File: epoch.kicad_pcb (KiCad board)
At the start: 4 copper layers, 28 x 34 mm, 36 parts, among them J1 USB_OTG, J2 CONN_01X05, P3 CONN_01X10, SW1 SW_Reset, SW2 SW_Up, SW3 SW_Middle, SW4 SW_Down, U1 MIC5219-3.3BM5, U2 ATSAMD21Ennc-AU, U3 DS3231MZ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

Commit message: Final connections
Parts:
- REF** (x4): footprint Connectors:1pin -> Connectors:1pin_nosilk
- SW1: footprint Buttons_Switches_SMD:SW_SPST_SKTDLDE010 -> Buttons_Switches_SMD:SW_SPST_B3U-3000P
- moved C4 38.7 mm to (121.7, 77.2), turned to 180 degrees
- moved R1 34.5 mm to (123.3, 79.2), turned to 180 degrees
- moved SW1 31.6 mm to (128.1, 79.9), turned to 270 degrees
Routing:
- net RESET: track 25.2 -> 44.5 mm, vias 2 -> 4
- net SCL: track 22.5 -> 31.7 mm, vias 2 -> 4
- net (+3.3): track 13.9 -> 21.1 mm, vias 0 -> 2
- net Net-(R1-Pad1): track 0.00 -> 3.95 mm
- net SPI_SI: track 28.7 -> 30.3 mm
- net SPI_CLK: track 21.3 -> 22.7 mm
- net (GND): track 33.6 -> 34.5 mm, vias 14 -> 15

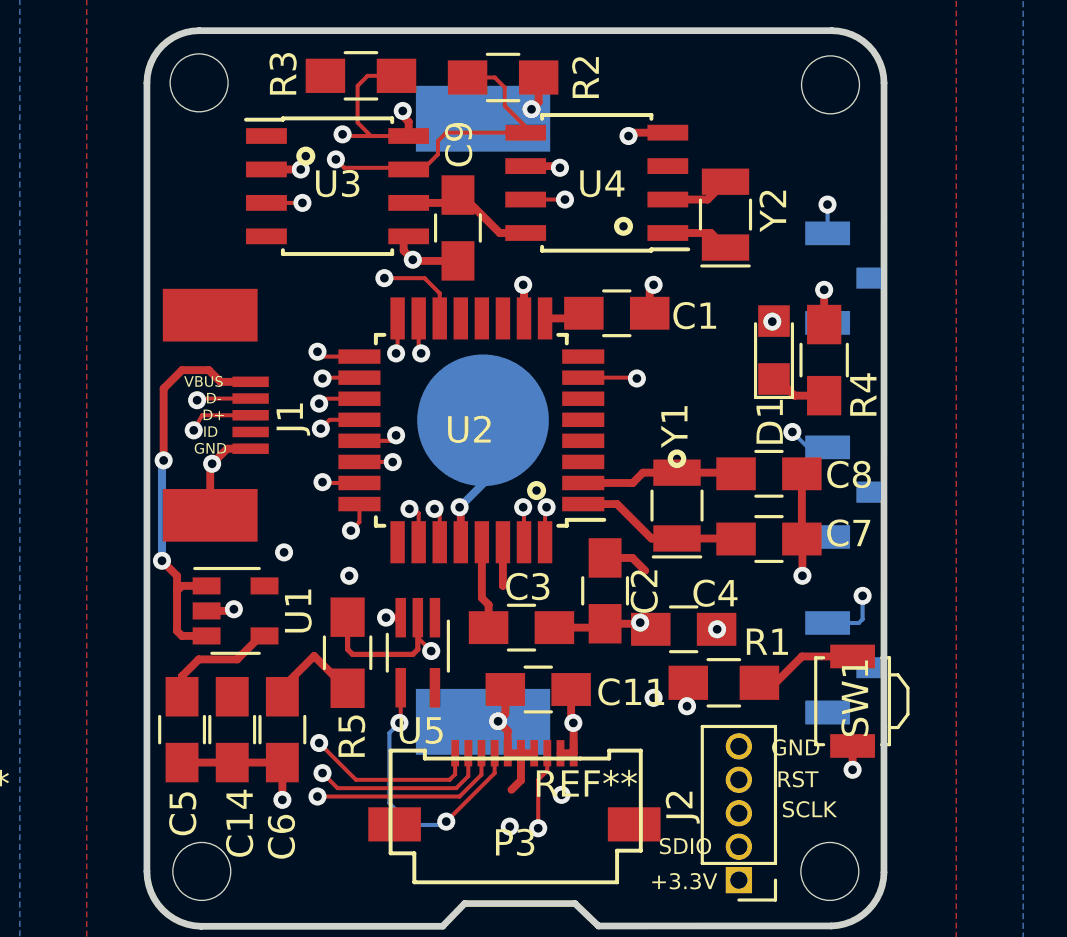
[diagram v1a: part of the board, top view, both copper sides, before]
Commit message: New buttons
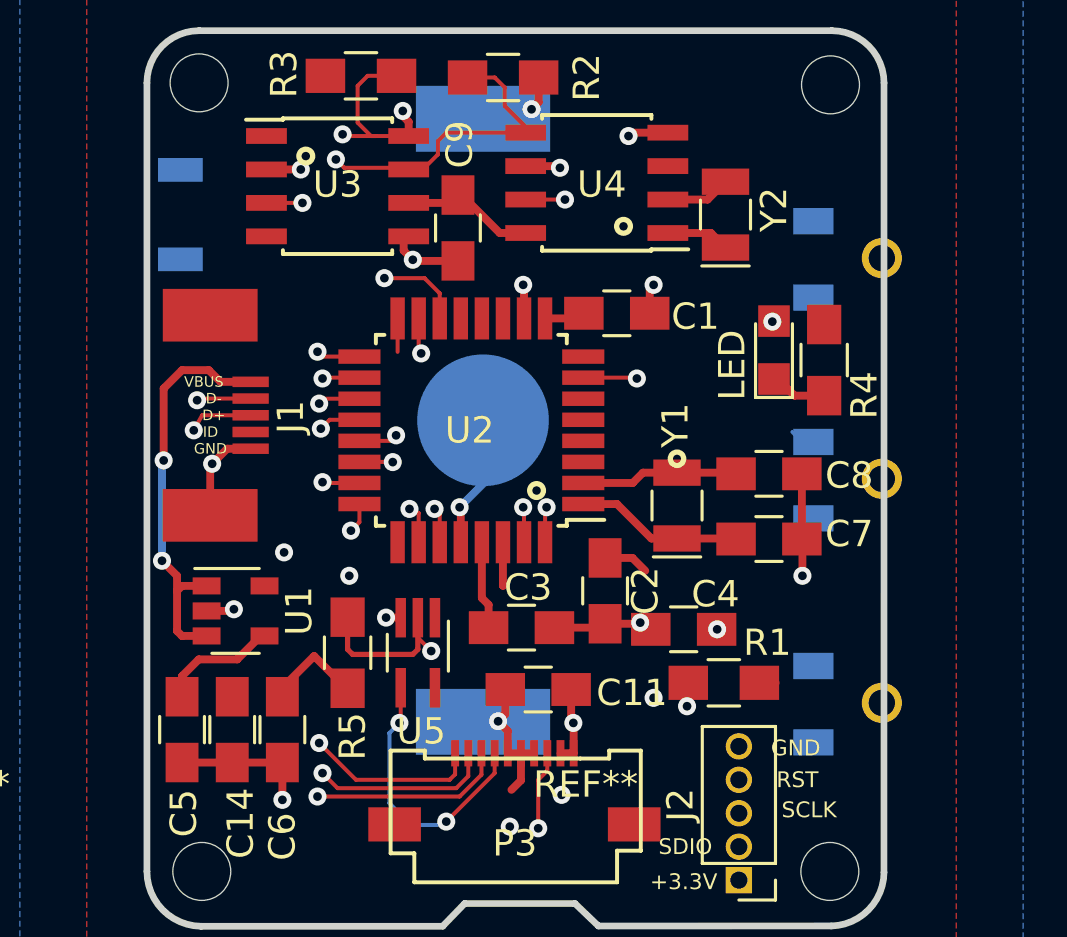
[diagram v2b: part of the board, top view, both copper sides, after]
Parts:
- SW1: moved to B.Cu
- SW2, SW3, SW4: footprint Buttons_Switches_SMD:SW_SPST_B3U-1100P -> Buttons_Switches_SMD:SW_SPDT_EBAY_3PIN_VERT
- moved SW1 31.5 mm to (102.6, 61.5)
- moved SW4 1.54 mm to (127.3, 80.0), turned to 90 degrees
- moved SW2 1.08 mm to (127.3, 63.1), turned to 90 degrees
- moved SW3 0.92 mm to (127.3, 71.5), turned to 90 degrees
- renumbered D1 to LED
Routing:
- net BUT_MID: track 19.5 -> 1.27 mm, vias 2 -> 0
- net (no net): track 0.00 -> 16.1 mm
- net BUT_UP: track 20.2 -> 6.58 mm, vias 2 -> 1
- net BUT_DWN: track 26.7 -> 16.2 mm, vias 2 -> 1
- net Net-(R1-Pad1): track 3.95 -> 0.62 mm
- net (GND): track 34.5 -> 33.9 mm, vias 15 -> 13

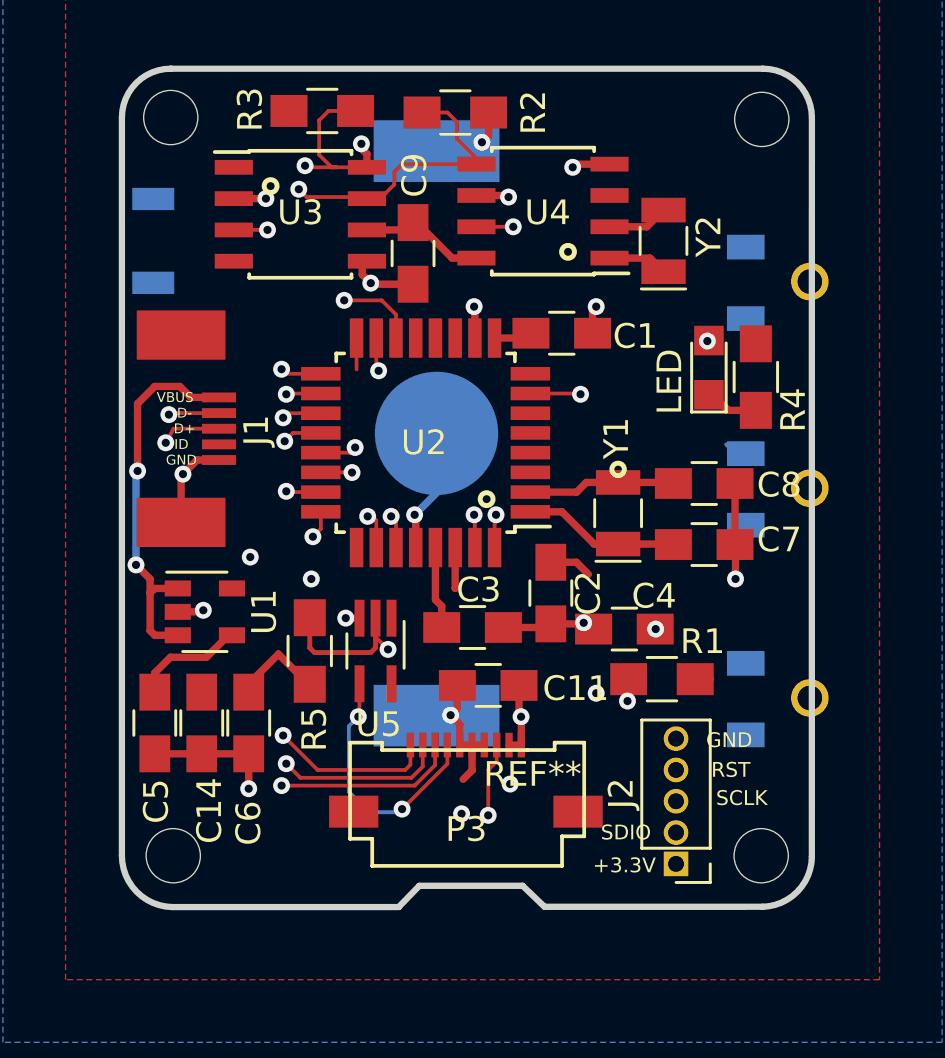
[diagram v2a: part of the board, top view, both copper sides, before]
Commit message: Update all buttons and re-route
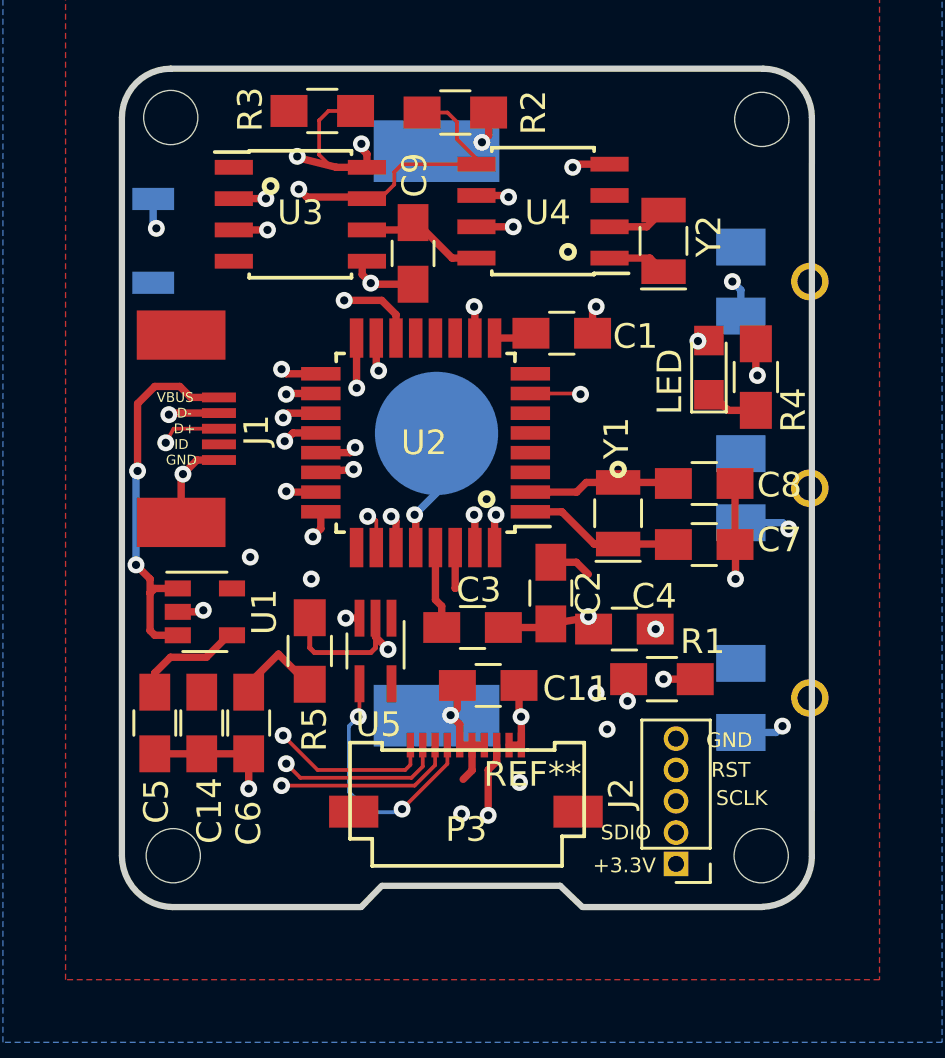
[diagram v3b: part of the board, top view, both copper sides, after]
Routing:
- net Net-(R1-Pad1): track 0.62 -> 40.2 mm, vias 0 -> 3
- net BUT_MID: track 1.27 -> 25.3 mm, vias 0 -> 2
- net (no net): track 16.1 -> 0.00 mm
- net BUT_DWN: track 16.2 -> 30.9 mm, vias 1 -> 2
- net BUT_UP: track 6.58 -> 18.8 mm, vias 1 -> 2
- net SCL: track 31.7 -> 34.0 mm
- net (GND): track 33.9 -> 35.4 mm, vias 13 -> 14
- net SDA: track 27.1 -> 28.0 mm
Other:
- outline, holes or cut-outs redrawn

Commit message: final.  Sent to manufacturer
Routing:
- net SPI_CLK: track 22.7 -> 21.9 mm
- net VCOM: track 10.5 -> 11.0 mm

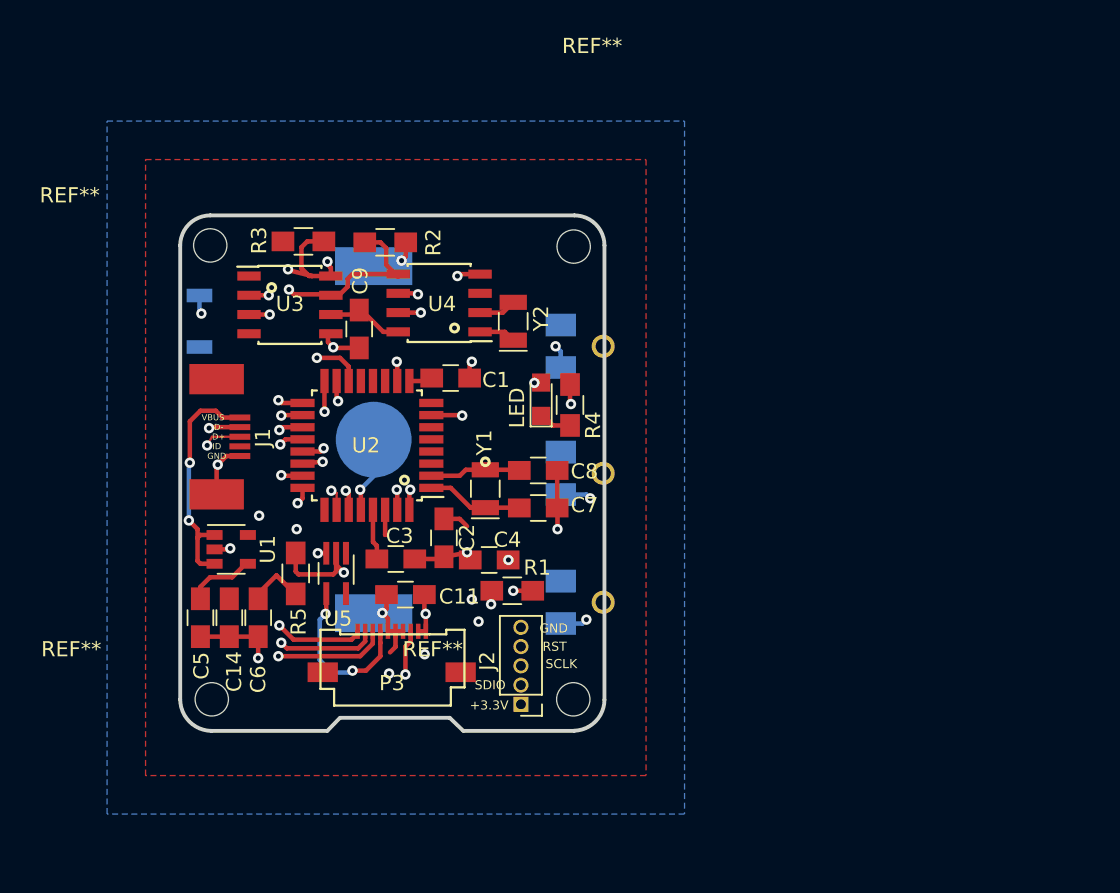
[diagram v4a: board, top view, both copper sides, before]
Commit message: Correct interrupt connections to pins that actually support interrupts
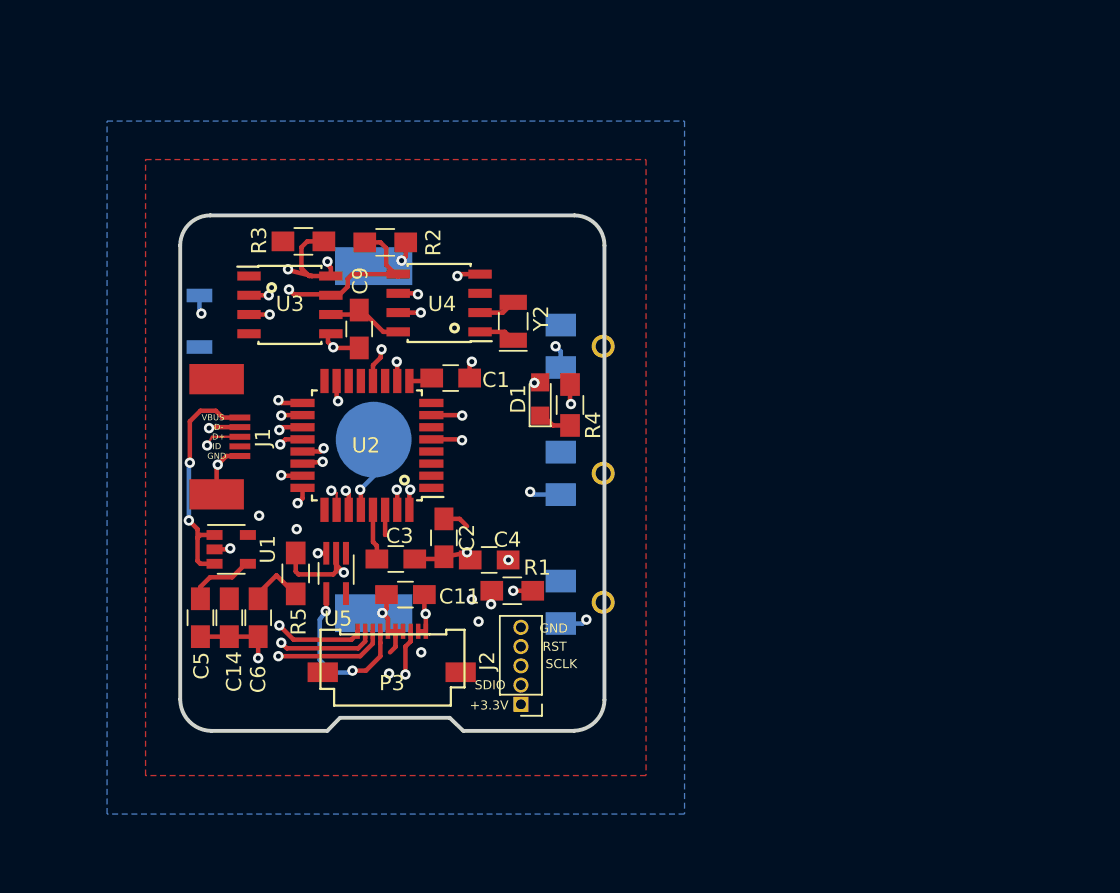
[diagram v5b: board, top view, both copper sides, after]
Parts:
- removed C7, C8: 18pF, Capacitors_SMD:C_0805_HandSoldering
- removed LED: LED, LEDs:LED_0805
- removed REF** (x4): 1pin, Connectors:1pin_nosilk
- removed Y1: 32.768kHz, Crystals:Crystal_SMD_EuroQuartz_EQ161-2pin_3.2x1.5mm
- added D1: LED, LEDs:LED_0805, F.Cu at (125.1, 66.6)
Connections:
- U2 pad 12: Net-(U2-Pad12) -> INTC
- U2 pad 14: INTC -> Net-(U2-Pad14)
- U2 pad 16: BUT_MID -> Net-(U2-Pad16)
- U2 pad 5: Net-(U2-Pad5) -> BUT_MID
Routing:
- net BUT_MID: track 25.3 -> 11.3 mm
- net Net-(U2-Pad1): track 6.35 -> 0.00 mm
- net Net-(U2-Pad2): track 5.98 -> 0.00 mm
- net (GND): track 35.4 -> 31.4 mm, vias 14 -> 13
- net INTC: track 8.95 -> 12.5 mm
- net BUT_DWN: track 30.9 -> 30.3 mm

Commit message: New version with crystal removed and 32Khz output into XTA of 2nd RTC
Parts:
- removed Y2: 32.768kHz, Crystals:Crystal_SMD_EuroQuartz_EQ161-2pin_3.2x1.5mm
- added R6: 10K, Resistors_SMD:R_0805_HandSoldering, F.Cu at (121.2, 56.3)
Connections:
- U3 pad 1: Net-(U3-Pad1) -> 32KHz
- U4 pad 1: Net-(U4-Pad1) -> 32KHz
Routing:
- net 32KHz: track 0.00 -> 32.0 mm, vias 0 -> 3
- net Net-(U4-Pad2): track 2.47 -> 0.00 mm
- net Net-(U4-Pad1): track 2.42 -> 0.00 mm
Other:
- board text added: "3.3V"
- board text removed: "+3.3V"

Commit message: Add drills back to PCB...Note this PCB does not include the battery protection switch which is shown in the schematic.
Not sure I have the PBC space to do this.  Maybe do a separate board.  Not sure.
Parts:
- added REF**: 1pin, Connectors:1pin_nosilk, F.Cu at (103.3, 56.5)
- added REF**: 1pin, Connectors:1pin_nosilk, F.Cu at (127.3, 56.5)
- added REF**: 1pin, Connectors:1pin_nosilk, F.Cu at (103.4, 86.4)
- added REF**: 1pin, Connectors:1pin_nosilk, F.Cu at (127.3, 86.4)
- moved SW1 20.2 mm to (102.6, 81.7)
- moved R3 0.06 mm to (109.5, 56.3), turned to 180 degrees
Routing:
- net Net-(R1-Pad1): track 40.2 -> 27.4 mm
- net (+3.3): track 21.1 -> 25.0 mm, vias 2 -> 3
- net SCL: track 34.0 -> 32.0 mm
- net (no net): track 0.00 -> 1.24 mm

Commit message: Revert "Add drills back to PCB...Note this PCB does not include the battery protection switch which is shown in the schematic."
This reverts commit 0a23e0f0d40f65d1b6f1174f50c74f54a2cdcd00.
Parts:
- removed REF** (x4): 1pin, Connectors:1pin_nosilk
- moved SW1 20.2 mm to (102.6, 61.5)
- moved R3 0.06 mm to (109.5, 56.2), turned to 0 degrees
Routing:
- net Net-(R1-Pad1): track 27.4 -> 40.2 mm
- net (+3.3): track 25.0 -> 21.1 mm, vias 3 -> 2
- net SCL: track 32.0 -> 34.0 mm
- net (no net): track 1.24 -> 0.00 mm
